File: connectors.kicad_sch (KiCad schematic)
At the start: 33 parts, among them J10 Conn_01x06, J11 Conn_01x04, J12 USB4085-GF-A, J13 Conn_01x02, J6 FTSH-107-01-L-DV-K-TR, J7 Conn_01x03, J8 Conn_01x02, J9 Conn_01x07, Q7 Si2302CDS

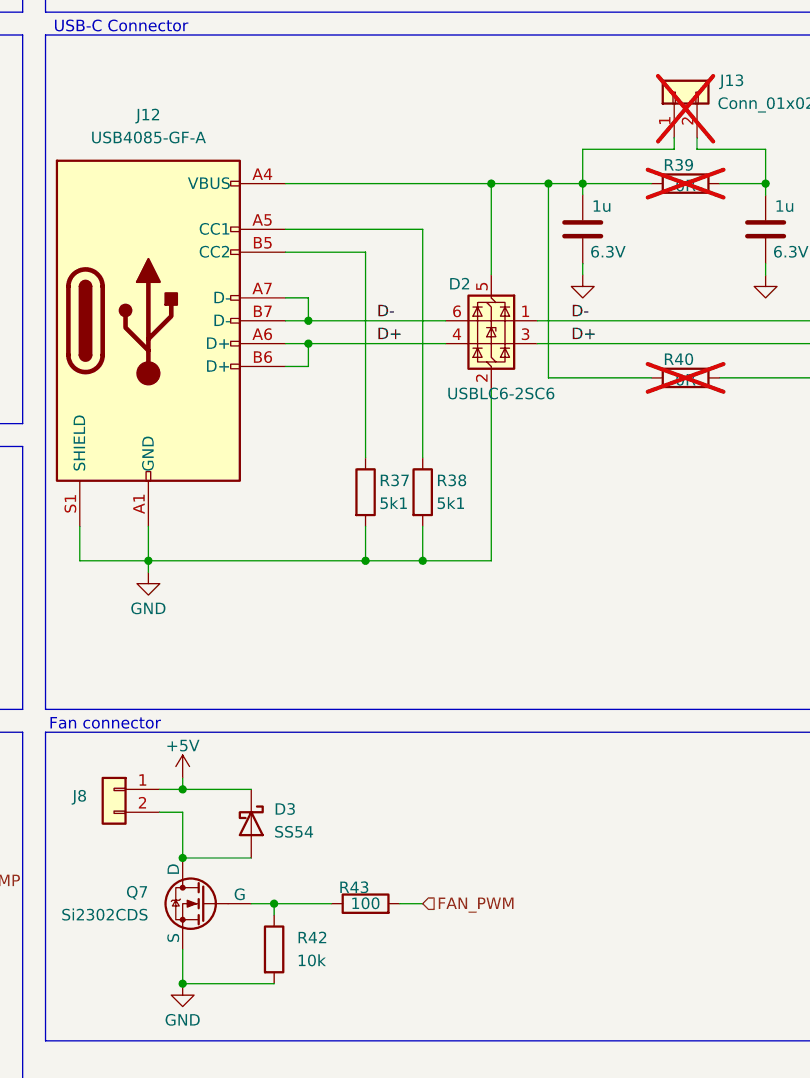
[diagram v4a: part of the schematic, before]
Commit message: Differential pair naming added. Duplicate footprint problem fixed.
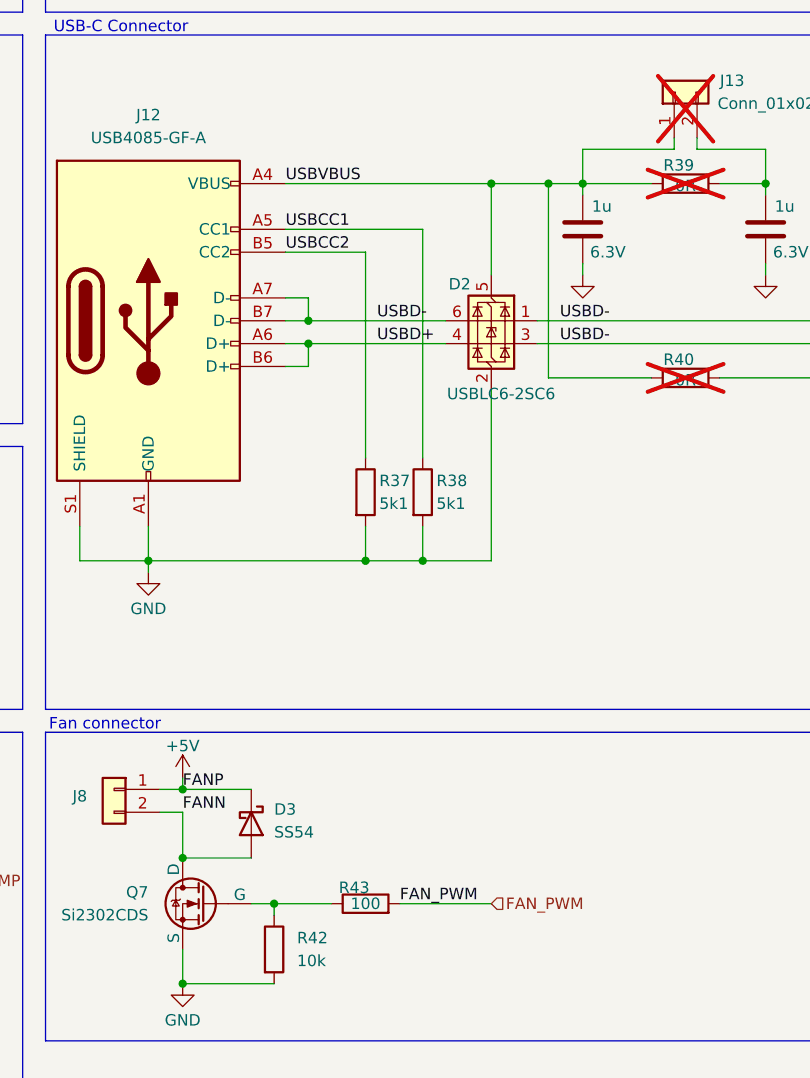
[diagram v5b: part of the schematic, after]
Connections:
- net D- is gone; now on net D+: D2.1 (I/O1), D2.6 (I/O1), J12.A7 (D-), J12.B7 (D-)
- net D+: no longer D2.4 (I/O2), J12.A6 (D+), J12.B6 (D+)
- net FANN: now reaches D3.2 (A), J8.2 (Pin_2), Q7.1 (D)
- net USBVBUS: now reaches C67.1, D2.5 (VBUS), J12.A4 (VBUS), J12.A9 (VBUS), J12.B4 (VBUS), J12.B9 (VBUS), J13.1 (Pin_1), R39.1, R40.1
- net USBCC1: now reaches J12.A5 (CC1), R38.1
- net USBCC2: now reaches J12.B5 (CC2), R37.1
- new net USBD+: D2.4 (I/O2), J12.A6 (D+), J12.B6 (D+)
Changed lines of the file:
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@@
 	(wire
 		(pts
-			(xy 143.51 149.86) (xy 146.05 149.86)
+			(xy 143.51 149.86) (xy 153.67 149.86)
 		)
 		(stroke
@@
 		)
 	)
-	(label "D-"
-		(at 162.56 85.09 0)
-		(effects
-			(font
-				(size 1.27 1.27)
-			)
-			(justify left bottom)
-		)
-	)
-	(label "D-"
+	(label "USBD-"
+		(at 161.29 87.63 0)
+		(effects
+			(font
+				(size 1.27 1.27)
+			)
+			(justify left bottom)
+		)
+	)
+	(label "USBCC1"
+		(at 130.81 74.93 0)
+		(effects
+			(font
+				(size 1.27 1.27)
+			)
+			(justify left bottom)
+		)
+	)
+	(label "FANN"
+		(at 119.38 139.7 0)
+		(effects
+			(font
+				(size 1.27 1.27)
+			)
+			(justify left bottom)
+		)
+	)
+	(label "USBD-"
 		(at 140.97 85.09 0)
 		(effects
@@
 		)
 	)
-	(label "D+"
-		(at 162.56 87.63 0)
-		(effects
-			(font
-				(size 1.27 1.27)
-			)
-			(justify left bottom)
-		)
-	)
-	(label "D+"
+	(label "FAN_PWM"
+		(at 143.51 149.86 0)
+		(effects
+			(font
+				(size 1.27 1.27)
+			)
+			(justify left bottom)
+		)
+	)
+	(label "USBVBUS"
+		(at 130.81 69.85 0)
+		(effects
+			(font
+				(size 1.27 1.27)
+			)
+			(justify left bottom)
+		)
+	)
+	(label "FANP"
+		(at 119.38 137.16 0)
+		(effects
+			(font
+				(size 1.27 1.27)
+			)
+			(justify left bottom)
+		)
+	)
+	(label "USBCC2"
+		(at 130.81 77.47 0)
+		(effects
+			(font
+				(size 1.27 1.27)
+			)
+			(justify left bottom)
+		)
+	)
+	(label "USBD-"
+		(at 161.29 85.09 0)
+		(effects
+			(font
+				(size 1.27 1.27)
+			)
+			(justify left bottom)
+		)
+	)
+	(label "USBD+"
 		(at 140.97 87.63 0)
 		(effects
@@
 	(hierarchical_label "FAN_PWM"
 		(shape input)
-		(at 146.05 149.86 0)
-		(effects
-			(font
+		(at 153.67 149.86 0)
+		(effects
+			(font

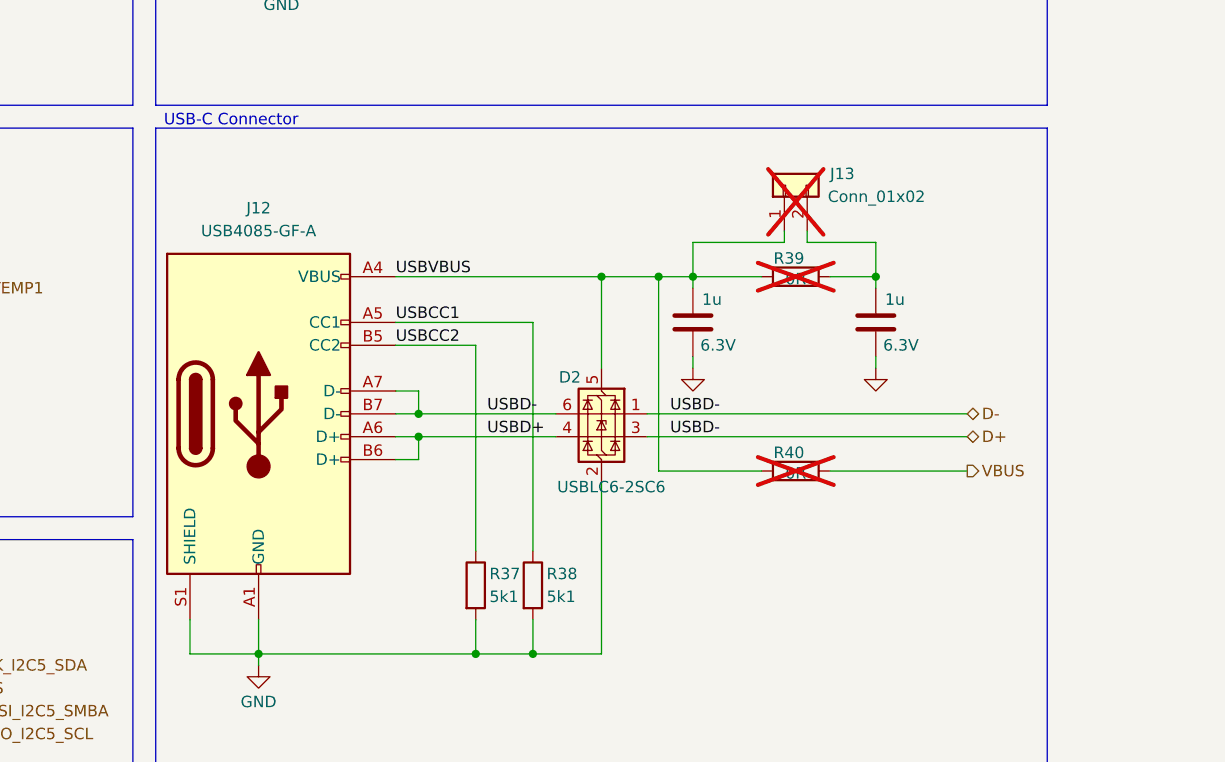
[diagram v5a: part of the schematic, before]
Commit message: added Net Classes  added +5V supply selection header
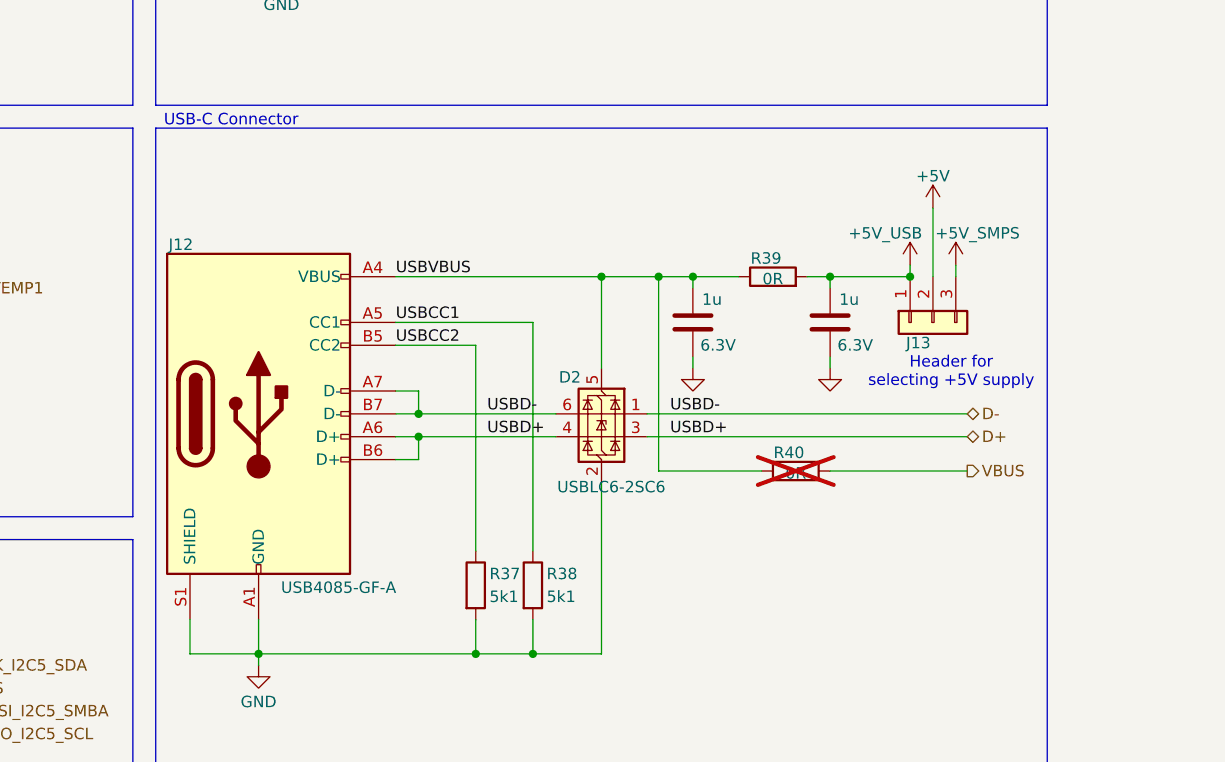
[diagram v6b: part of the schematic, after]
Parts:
- removed J13: Conn_01x02, Connector_PinHeader_1.00mm:PinHeader_1x02_P1.00mm_Vertical, symbol Connector_Generic:Conn_01x02
- added J13: Conn_01x03, Connector_PinHeader_1.00mm:PinHeader_1x03_P1.00mm_Vertical, symbol Connector_Generic:Conn_01x03
- R39: now fitted; now in the parts list
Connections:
- net USBD+ is gone; now on net D+: D2.4 (I/O2), J12.A6 (D+), J12.B6 (D+)
- net +5V: now also J13.2 (Pin_2)
- net D+: no longer D2.1 (I/O1), D2.6 (I/O1), J12.A7 (D-), J12.B7 (D-)
- net +5V_USB: now reaches C68.1, R39.2
- net +5V_USB: now also J13.1 (Pin_1)
- new net +5V_SMPS: J13.3 (Pin_3)
- new net D-: D2.1 (I/O1), D2.6 (I/O1), J12.A7 (D-), J12.B7 (D-)
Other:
- note added: "Header for selecting +5V supply"

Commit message: WiP layout
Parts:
- added J14: Conn_01x03, Connector:FanPinHeader_1x03_P2.54mm_Vertical, symbol Connector_Generic:Conn_01x03
- added R50: 100, Resistor_SMD:R_0402_1005Metric, symbol Device:R
- R34, R35, R36, R42: footprint Resistor_SMD:R_0603_1608Metric -> Resistor_SMD:R_0402_1005Metric; LCSC C25804 -> C25744
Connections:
- net +5V: now also J14.2 (Pin_2)
- net GND: now also R42.1, J14.3 (Pin_3); no longer R42.2
- net HALL_IN2: now reaches J10.4 (Pin_4), R31.2, R35.1
- net FAN_Q_GATE: now reaches Q7.2 (G), R43.1
- net FAN_Q_GATE: now also R42.2; no longer R42.1
- net HALL_IN1: now reaches J10.3 (Pin_3), R29.2, R34.1
- net HALL_IN3: now reaches J10.5 (Pin_5), R33.2, R36.1
- new net SERVO: R50.2
- new net SERVO_IN: J14.1 (Pin_1), R50.1
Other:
- note added: "Header might be to weak for 3.5A"
- note added: "Servo"
- moved on the sheet: R31, R33, R43

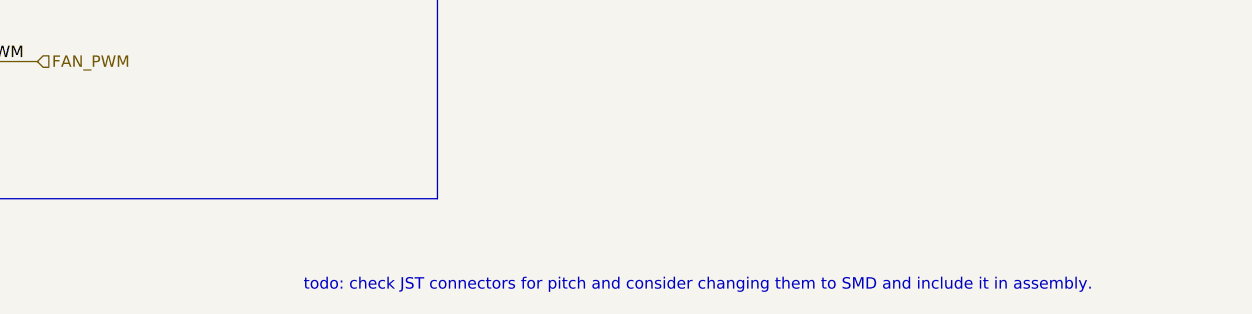
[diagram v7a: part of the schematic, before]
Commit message: added over current protection triggers (adjustable)
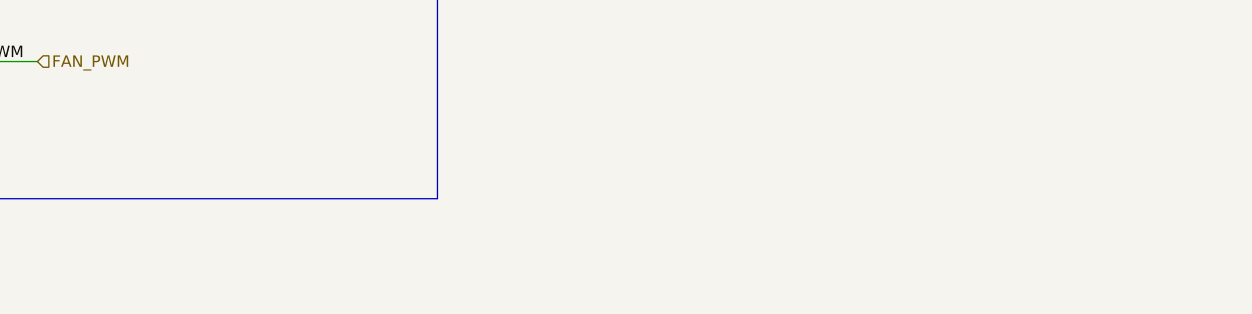
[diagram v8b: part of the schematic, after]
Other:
- note removed: "todo: check JST connectors for pitch and consider changing them to SMD and include it in assembly."
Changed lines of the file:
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@@
-		)
-	)
-	(text "todo: check JST connectors for pitch and consider changing them to SMD and include it in assembly."
-		(exclude_from_sim no)
-		(at 232.156 174.752 0)
-		(effects
-			(font
-				(size 1.27 1.27)
-			)
 		)
 	)
